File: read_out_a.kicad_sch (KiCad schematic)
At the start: 26 parts, among them J1 Bus_PCI_Express_x16, U10 74LS541, U11 74LS541, U12 74LS541, U13 74LS541, U14 74LS541, U15 74LS541, U16 74LS541, U17 74LS30, U18 74LS04, U9 74LS541

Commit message: Current progress.  Working on laying out the latched bus.
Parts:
- C12: renamed from C9; footprint (none) -> Capacitor_SMD:C_0805_2012Metric_Pad1.18x1.45mm_HandSolder
- C13: renamed from C10; footprint (none) -> Capacitor_SMD:C_0805_2012Metric_Pad1.18x1.45mm_HandSolder
- C14: renamed from C11; footprint (none) -> Capacitor_SMD:C_0805_2012Metric_Pad1.18x1.45mm_HandSolder
- C15: renamed from C12; footprint (none) -> Capacitor_SMD:C_0805_2012Metric_Pad1.18x1.45mm_HandSolder
- C16: renamed from C13; footprint (none) -> Capacitor_SMD:C_0805_2012Metric_Pad1.18x1.45mm_HandSolder
- C17: renamed from C14; footprint (none) -> Capacitor_SMD:C_0805_2012Metric_Pad1.18x1.45mm_HandSolder
- C18: renamed from C15; footprint (none) -> Capacitor_SMD:C_0805_2012Metric_Pad1.18x1.45mm_HandSolder
- C19: renamed from C16; footprint (none) -> Capacitor_SMD:C_0805_2012Metric_Pad1.18x1.45mm_HandSolder
- C20: renamed from C17; footprint (none) -> Capacitor_SMD:C_0805_2012Metric_Pad1.18x1.45mm_HandSolder
- C21: renamed from C18; footprint (none) -> Capacitor_SMD:C_0805_2012Metric_Pad1.18x1.45mm_HandSolder
- JP10: renamed from JP5; footprint (none) -> Jumper:SolderJumper-3_P1.3mm_Open_RoundedPad1.0x1.5mm
- JP6: renamed from JP1; footprint (none) -> Jumper:SolderJumper-3_P1.3mm_Open_RoundedPad1.0x1.5mm
- JP7: renamed from JP2; footprint (none) -> Jumper:SolderJumper-3_P1.3mm_Open_RoundedPad1.0x1.5mm
- JP8: renamed from JP3; footprint (none) -> Jumper:SolderJumper-3_P1.3mm_Open_RoundedPad1.0x1.5mm
- JP9: renamed from JP4; footprint (none) -> Jumper:SolderJumper-3_P1.3mm_Open_RoundedPad1.0x1.5mm
- U12: renamed from U9; footprint (none) -> Package_SO:SOIC-20W_7.5x12.8mm_P1.27mm
- U13: renamed from U10; footprint (none) -> Package_SO:SOIC-20W_7.5x12.8mm_P1.27mm
- U14: renamed from U11; footprint (none) -> Package_SO:SOIC-20W_7.5x12.8mm_P1.27mm
- U15: renamed from U12; footprint (none) -> Package_SO:SOIC-20W_7.5x12.8mm_P1.27mm
- U16: renamed from U13; footprint (none) -> Package_SO:SOIC-20W_7.5x12.8mm_P1.27mm
- U17: renamed from U14; footprint (none) -> Package_SO:SOIC-20W_7.5x12.8mm_P1.27mm
- U18: renamed from U15; footprint (none) -> Package_SO:SOIC-20W_7.5x12.8mm_P1.27mm
- U19: renamed from U16; footprint (none) -> Package_SO:SOIC-20W_7.5x12.8mm_P1.27mm
- U20: renamed from U18; footprint (none) -> Package_SO:SOIC-14_3.9x8.7mm_P1.27mm
- U21: renamed from U17; footprint (none) -> Package_SO:SOIC-14_3.9x8.7mm_P1.27mm
- renumbered J1 to J2
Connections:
- net CLK_PH0: no longer names the net of J2.A13 (REFCLK+)
- net CLK_PH1: no longer names the net of J2.A14 (REFCLK-)
- net latched00 renamed latched0
- net latched01 renamed latched1
- net latched02 renamed latched2
- net latched03 renamed latched3
- net latched04 renamed latched4
- net latched05 renamed latched5
- net latched06 renamed latched6
- net latched07 renamed latched7
- net latched08 renamed latched8
- net latched09 renamed latched9
- net read_a00 renamed read_a0
- net read_a01 renamed read_a1
- net read_a02 renamed read_a2
- net read_a03 renamed read_a3
- net read_a04 renamed read_a4
- net read_a05 renamed read_a5
- net read_a06 renamed read_a6
- net read_a07 renamed read_a7
- net read_a08 renamed read_a8
- net read_a09 renamed read_a9
- net ~{RST}: no longer names the net of J2.A11 (~{PERST})
- no-connect marks 17 -> 20

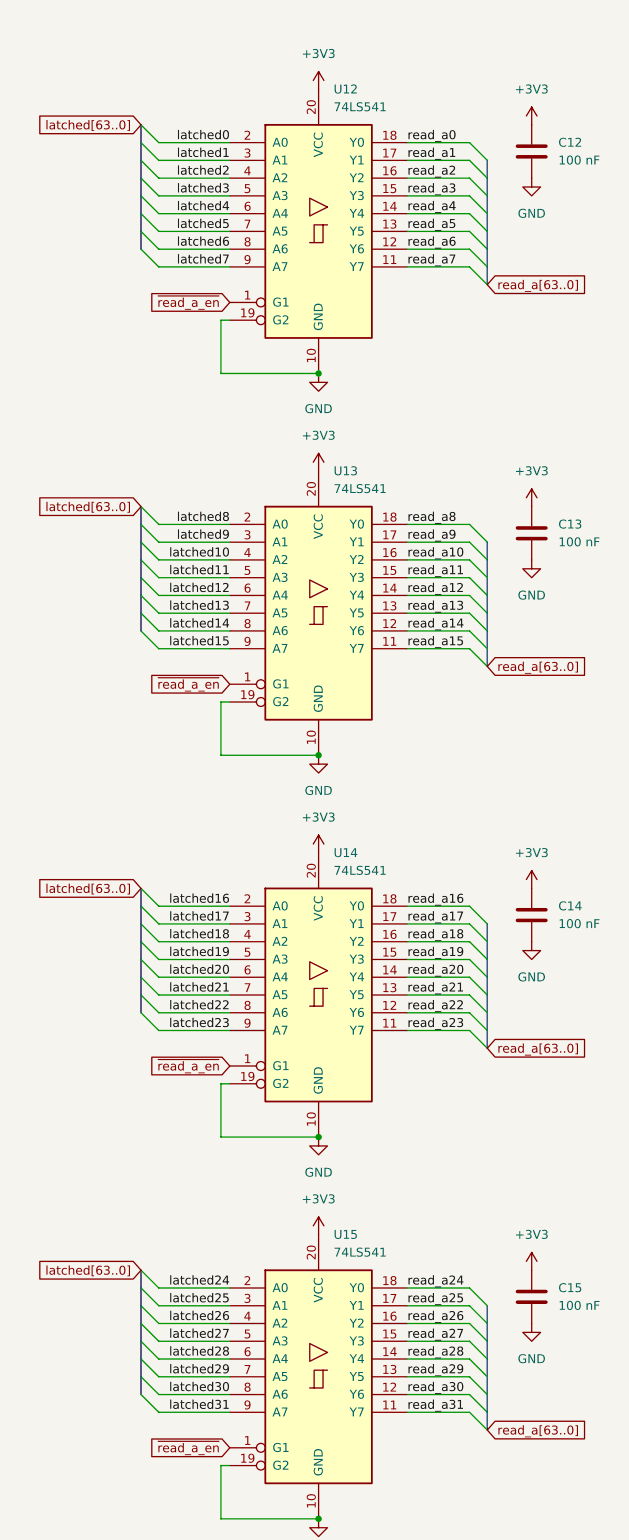
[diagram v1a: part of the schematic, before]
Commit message: Read A Port mostly routed.
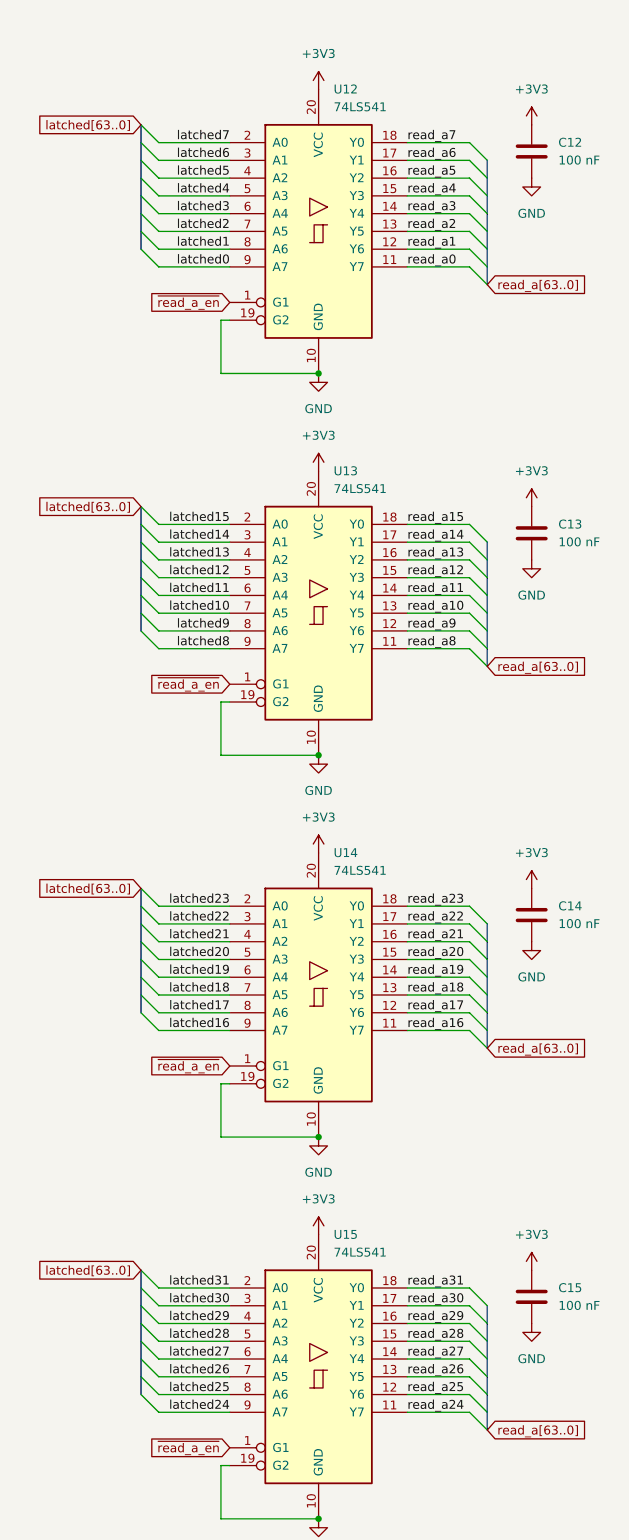
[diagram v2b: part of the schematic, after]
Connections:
- net latched0: now also U12.9 (A7); no longer U12.2 (A0)
- net latched1: now also U12.8 (A6); no longer U12.3 (A1)
- net latched10: now also U13.7 (A5); no longer U13.4 (A2)
- net latched11: now also U13.6 (A4); no longer U13.5 (A3)
- net latched12: now also U13.5 (A3); no longer U13.6 (A4)
- net latched13: now also U13.4 (A2); no longer U13.7 (A5)
- net latched14: now also U13.3 (A1); no longer U13.8 (A6)
- net latched15: now also U13.2 (A0); no longer U13.9 (A7)
- net latched16: now also U14.9 (A7); no longer U14.2 (A0)
- net latched17: now also U14.8 (A6); no longer U14.3 (A1)
- net latched18: now also U14.7 (A5); no longer U14.4 (A2)
- net latched19: now also U14.6 (A4); no longer U14.5 (A3)
- net latched2: now also U12.7 (A5); no longer U12.4 (A2)
- net latched20: now also U14.5 (A3); no longer U14.6 (A4)
- net latched21: now also U14.4 (A2); no longer U14.7 (A5)
- net latched22: now also U14.3 (A1); no longer U14.8 (A6)
- net latched23: now also U14.2 (A0); no longer U14.9 (A7)
- net latched24: now also U15.9 (A7); no longer U15.2 (A0)
- net latched25: now also U15.8 (A6); no longer U15.3 (A1)
- net latched26: now also U15.7 (A5); no longer U15.4 (A2)
- net latched27: now also U15.6 (A4); no longer U15.5 (A3)
- net latched28: now also U15.5 (A3); no longer U15.6 (A4)
- net latched29: now also U15.4 (A2); no longer U15.7 (A5)
- net latched3: now also U12.6 (A4); no longer U12.5 (A3)
- net latched30: now also U15.3 (A1); no longer U15.8 (A6)
- net latched31: now also U15.2 (A0); no longer U15.9 (A7)
- net latched4: now also U12.5 (A3); no longer U12.6 (A4)
- net latched5: now also U12.4 (A2); no longer U12.7 (A5)
- net latched6: now also U12.3 (A1); no longer U12.8 (A6)
- net latched7: now also U12.2 (A0); no longer U12.9 (A7)
- net latched8: now also U13.9 (A7); no longer U13.2 (A0)
- net latched9: now also U13.8 (A6); no longer U13.3 (A1)
- net read_a0: now also U12.11 (Y7); no longer U12.18 (Y0)
- net read_a1: now also U12.12 (Y6); no longer U12.17 (Y1)
- net read_a10: now also U13.13 (Y5); no longer U13.16 (Y2)
- net read_a11: now also U13.14 (Y4); no longer U13.15 (Y3)
- net read_a12: now also U13.15 (Y3); no longer U13.14 (Y4)
- net read_a13: now also U13.16 (Y2); no longer U13.13 (Y5)
- net read_a14: now also U13.17 (Y1); no longer U13.12 (Y6)
- net read_a15: now also U13.18 (Y0); no longer U13.11 (Y7)
- net read_a16: now also U14.11 (Y7); no longer U14.18 (Y0)
- net read_a17: now also U14.12 (Y6); no longer U14.17 (Y1)
- net read_a18: now also U14.13 (Y5); no longer U14.16 (Y2)
- net read_a19: now also U14.14 (Y4); no longer U14.15 (Y3)
- net read_a2: now also U12.13 (Y5); no longer U12.16 (Y2)
- net read_a20: now also U14.15 (Y3); no longer U14.14 (Y4)
- net read_a21: now also U14.16 (Y2); no longer U14.13 (Y5)
- net read_a22: now also U14.17 (Y1); no longer U14.12 (Y6)
- net read_a23: now also U14.18 (Y0); no longer U14.11 (Y7)
- net read_a24: now also U15.11 (Y7); no longer U15.18 (Y0)
- net read_a25: now also U15.12 (Y6); no longer U15.17 (Y1)
- net read_a26: now also U15.13 (Y5); no longer U15.16 (Y2)
- net read_a27: now also U15.14 (Y4); no longer U15.15 (Y3)
- net read_a28: now also U15.15 (Y3); no longer U15.14 (Y4)
- net read_a29: now also U15.16 (Y2); no longer U15.13 (Y5)
- net read_a3: now also U12.14 (Y4); no longer U12.15 (Y3)
- net read_a30: now also U15.17 (Y1); no longer U15.12 (Y6)
- net read_a31: now also U15.18 (Y0); no longer U15.11 (Y7)
- net read_a4: now also U12.15 (Y3); no longer U12.14 (Y4)
- net read_a5: now also U12.16 (Y2); no longer U12.13 (Y5)
- net read_a6: now also U12.17 (Y1); no longer U12.12 (Y6)
- net read_a7: now also U12.18 (Y0); no longer U12.11 (Y7)
- net read_a8: now also U13.11 (Y7); no longer U13.18 (Y0)
- net read_a9: now also U13.12 (Y6); no longer U13.17 (Y1)
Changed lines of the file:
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@@
 	)
 	(label "latched6"
-		(at 73.66 53.34 180)
+		(at 73.66 40.64 180)
 		(effects
 			(font
@@
 	)
 	(label "latched29"
-		(at 73.66 214.63 180)
+		(at 73.66 207.01 180)
 		(effects
 			(font
@@
 	)
 	(label "latched18"
-		(at 73.66 152.4 180)
+		(at 73.66 160.02 180)
 		(effects
 			(font
@@
 	)
 	(label "read_a6"
-		(at 99.06 53.34 0)
+		(at 99.06 40.64 0)
 		(effects
 			(font
@@
 	)
 	(label "read_a0"
-		(at 99.06 38.1 0)
+		(at 99.06 55.88 0)
 		(effects
 			(font
@@
 	)
 	(label "latched12"
-		(at 73.66 102.87 180)
+		(at 73.66 100.33 180)
 		(effects
 			(font
@@
 	)
 	(label "read_a5"
-		(at 99.06 50.8 0)
+		(at 99.06 43.18 0)
 		(effects
 			(font
@@
 	)
 	(label "latched14"
-		(at 73.66 107.95 180)
+		(at 73.66 95.25 180)
 		(effects
 			(font
@@
 	)
 	(label "read_a9"
-		(at 99.06 95.25 0)
+		(at 99.06 107.95 0)
 		(effects
 			(font
@@
 	)
 	(label "read_a15"
-		(at 99.06 110.49 0)
+		(at 99.06 92.71 0)
 		(effects
 			(font
@@
 	)
 	(label "latched15"
-		(at 73.66 110.49 180)
+		(at 73.66 92.71 180)
 		(effects
 			(font
@@
 	)
 	(label "latched17"
-		(at 73.66 149.86 180)
+		(at 73.66 162.56 180)
 		(effects
 			(font
@@
 	)
 	(label "latched27"
-		(at 73.66 209.55 180)
+		(at 73.66 212.09 180)
 		(effects
 			(font
@@
 	)
 	(label "latched13"
-		(at 73.66 105.41 180)
+		(at 73.66 97.79 180)
 		(effects
 			(font
@@
 	)
 	(label "latched19"
-		(at 73.66 154.94 180)
+		(at 73.66 157.48 180)
 		(effects
 			(font
@@
 	)
 	(label "latched9"
-		(at 73.66 95.25 180)
+		(at 73.66 107.95 180)
 		(effects
 			(font
@@
 	)
 	(label "read_a12"
-		(at 99.06 102.87 0)
+		(at 99.06 100.33 0)
 		(effects
 			(font
@@
 	)
 	(label "latched7"
-		(at 73.66 55.88 180)
+		(at 73.66 38.1 180)
 		(effects
 			(font
@@
 	)
 	(label "latched28"
-		(at 73.66 212.09 180)
+		(at 73.66 209.55 180)
 		(effects
 			(font
@@
 	)
 	(label "latched24"
-		(at 73.66 201.93 180)
+		(at 73.66 219.71 180)
 		(effects
 			(font
@@
 	)
 	(label "read_a7"
-		(at 99.06 55.88 0)
+		(at 99.06 38.1 0)
 		(effects
 			(font
@@
 	)
 	(label "latched11"
-		(at 73.66 100.33 180)
+		(at 73.66 102.87 180)
 		(effects
 			(font
@@
 	)
 	(label "read_a13"
-		(at 99.06 105.41 0)
+		(at 99.06 97.79 0)
 		(effects
 			(font
@@
 	)
 	(label "read_a28"
-		(at 99.06 212.09 0)
+		(at 99.06 209.55 0)
 		(effects
 			(font
@@
 	)
 	(label "latched20"
-		(at 73.66 157.48 180)
+		(at 73.66 154.94 180)
 		(effects
 			(font
@@
 	)
 	(label "read_a10"
-		(at 99.06 97.79 0)
+		(at 99.06 105.41 0)
 		(effects
 			(font
@@
 	)
 	(label "latched22"
-		(at 73.66 162.56 180)
+		(at 73.66 149.86 180)
 		(effects
 			(font
@@
 	)
 	(label "latched21"
-		(at 73.66 160.02 180)
+		(at 73.66 152.4 180)
 		(effects
 			(font
@@
 	)
 	(label "latched5"
-		(at 73.66 50.8 180)
+		(at 73.66 43.18 180)
 		(effects
 			(font
@@
 	)
 	(label "read_a11"
-		(at 99.06 100.33 0)
+		(at 99.06 102.87 0)
 		(effects
 			(font
@@
 	)
 	(label "latched8"
-		(at 73.66 92.71 180)
+		(at 73.66 110.49 180)
 		(effects
 			(font
@@
 	)
 	(label "latched16"
-		(at 73.66 147.32 180)
+		(at 73.66 165.1 180)
 		(effects
 			(font
@@
 	)
 	(label "read_a29"
-		(at 99.06 214.63 0)
+		(at 99.06 207.01 0)
 		(effects
 			(font
@@
 	)
 	(label "read_a2"
-		(at 99.06 43.18 0)
+		(at 99.06 50.8 0)
 		(effects
 			(font
@@
 	)
 	(label "read_a17"
-		(at 99.06 149.86 0)
+		(at 99.06 162.56 0)
 		(effects
 			(font
@@
 	)
 	(label "latched3"
-		(at 73.66 45.72 180)
+		(at 73.66 48.26 180)
 		(effects
 			(font
@@
 	)
 	(label "latched10"
-		(at 73.66 97.79 180)
+		(at 73.66 105.41 180)
 		(effects
 			(font
@@
 	)
 	(label "latched0"
-		(at 73.66 38.1 180)
+		(at 73.66 55.88 180)
 		(effects
 			(font
@@
 	)
 	(label "latched25"
-		(at 73.66 204.47 180)
+		(at 73.66 217.17 180)
 		(effects
 			(font
@@
 	)
 	(label "latched26"
-		(at 73.66 207.01 180)
+		(at 73.66 214.63 180)
 		(effects
 			(font
@@
 	)
 	(label "read_a31"
-		(at 99.06 219.71 0)
+		(at 99.06 201.93 0)
 		(effects
 			(font
@@
 	)
 	(label "read_a8"
-		(at 99.06 92.71 0)
+		(at 99.06 110.49 0)
 		(effects
 			(font
@@
 	)
 	(label "read_a16"
-		(at 99.06 147.32 0)
+		(at 99.06 165.1 0)
 		(effects
 			(font
@@
 	)
 	(label "read_a1"
-		(at 99.06 40.64 0)
+		(at 99.06 53.34 0)
 		(effects
 			(font
@@
 	)
 	(label "read_a23"
-		(at 99.06 165.1 0)
+		(at 99.06 147.32 0)
 		(effects
 			(font
@@
 	)
 	(label "read_a30"
-		(at 99.06 217.17 0)
+		(at 99.06 204.47 0)
 		(effects
 			(font
@@
 	)
 	(label "read_a24"
-		(at 99.06 201.93 0)
+		(at 99.06 219.71 0)
 		(effects
 			(font
@@
 	)
 	(label "latched4"
-		(at 73.66 48.26 180)
+		(at 73.66 45.72 180)
 		(effects
 			(font
@@
 	)
 	(label "read_a19"
-		(at 99.06 154.94 0)
+		(at 99.06 157.48 0)
 		(effects
 			(font
@@
 	)
 	(label "latched23"
-		(at 73.66 165.1 180)
+		(at 73.66 147.32 180)
 		(effects
 			(font
@@
 	)
 	(label "read_a27"
-		(at 99.06 209.55 0)
+		(at 99.06 212.09 0)
 		(effects
 			(font
@@
 	)
 	(label "read_a20"
-		(at 99.06 157.48 0)
+		(at 99.06 154.94 0)
 		(effects
 			(font
@@
 	)
 	(label "latched1"
-		(at 73.66 40.64 180)
+		(at 73.66 53.34 180)
 		(effects
 			(font
@@
 	)
 	(label "read_a25"
-		(at 99.06 204.47 0)
+		(at 99.06 217.17 0)
 		(effects
 			(font
@@
 	)
 	(label "latched30"
-		(at 73.66 217.17 180)
+		(at 73.66 204.47 180)
 		(effects
 			(font
@@
 	)
 	(label "latched2"
-		(at 73.66 43.18 180)
+		(at 73.66 50.8 180)
 		(effects
 			(font
@@
 	)
 	(label "read_a14"
-		(at 99.06 107.95 0)
+		(at 99.06 95.25 0)
 		(effects
 			(font
@@
 	)
 	(label "read_a18"
-		(at 99.06 152.4 0)
+		(at 99.06 160.02 0)
 		(effects
 			(font
@@
 	)
 	(label "read_a4"
-		(at 99.06 48.26 0)
+		(at 99.06 45.72 0)
 		(effects
 			(font
@@
 	)
 	(label "read_a21"
-		(at 99.06 160.02 0)
+		(at 99.06 152.4 0)
 		(effects
 			(font
@@
 	)
 	(label "read_a26"
-		(at 99.06 207.01 0)
+		(at 99.06 214.63 0)
 		(effects
 			(font
@@
 	)
 	(label "read_a3"
-		(at 99.06 45.72 0)
+		(at 99.06 48.26 0)
 		(effects
 			(font
@@
 	)
 	(label "read_a22"
-		(at 99.06 162.56 0)
+		(at 99.06 149.86 0)
 		(effects
 			(font
@@
 	)
 	(label "latched31"
-		(at 73.66 219.71 180)
-		(effects
-			(font
+		(at 73.66 201.93 180)
+		(effects
+			(font

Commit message: Getting close to done with Read A Port.
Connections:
- net read_a_en: now also U20.6; no longer U20.12
- net read_a_sel2: now also U20.13; no longer U20.5
- net read_a_sel3: now also U20.11; no longer U20.9
- net read_a_sel4: now also U20.9; no longer U20.11
- net ~{read_a_en}: now also U20.5; no longer U20.13
- net at U20.8: now also JP10.3 (B); no longer JP9.3 (B)
- net at JP8.3 (B): now also U20.12; no longer U20.6
- net at U20.10: now also JP9.3 (B); no longer JP10.3 (B)
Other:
- moved on the sheet: U20C, U20D, U20E, U20F
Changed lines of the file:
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@@
 	(symbol
 		(lib_id "74xx:74LS04")
-		(at 265.43 129.54 0)
+		(at 265.43 158.75 0)
 		(unit 4)
 		(exclude_from_sim no)
@@
 		(fields_autoplaced yes)
 		(property "Reference" "U20"
-			(at 265.43 120.65 0)
+			(at 265.43 149.86 0)
 			(effects
 				(font
@@
 		)
 		(property "Value" "74LS04"
-			(at 265.43 123.19 0)
+			(at 265.43 152.4 0)
 			(effects
 				(font
@@
 		)
 		(property "Footprint" "Package_SO:SOIC-14_3.9x8.7mm_P1.27mm"
-			(at 265.43 129.54 0)
+			(at 265.43 158.75 0)
 			(effects
 				(font
@@
 		)
 		(property "Datasheet" "http://www.ti.com/lit/gpn/sn74LS04"
-			(at 265.43 129.54 0)
+			(at 265.43 158.75 0)
 			(effects
 				(font
@@
 		)
 		(property "Description" "Hex Inverter"
-			(at 265.43 129.54 0)
+			(at 265.43 158.75 0)
 			(effects
 				(font
@@
 	(symbol
 		(lib_id "74xx:74LS04")
-		(at 265.43 100.33 0)
+		(at 321.31 38.1 0)
 		(unit 3)
 		(exclude_from_sim no)
@@
 		(fields_autoplaced yes)
 		(property "Reference" "U20"
-			(at 265.43 91.44 0)
+			(at 321.31 29.21 0)
 			(effects
 				(font
@@
 		)
 		(property "Value" "74LS04"
-			(at 265.43 93.98 0)
+			(at 321.31 31.75 0)
 			(effects
 				(font
@@
 		)
 		(property "Footprint" "Package_SO:SOIC-14_3.9x8.7mm_P1.27mm"
-			(at 265.43 100.33 0)
+			(at 321.31 38.1 0)
 			(effects
 				(font
@@
 		)
 		(property "Datasheet" "http://www.ti.com/lit/gpn/sn74LS04"
-			(at 265.43 100.33 0)
+			(at 321.31 38.1 0)
 			(effects
 				(font
@@
 		)
 		(property "Description" "Hex Inverter"
-			(at 265.43 100.33 0)
+			(at 321.31 38.1 0)
 			(effects
 				(font
@@
 	(symbol
 		(lib_id "74xx:74LS04")
-		(at 265.43 158.75 0)
+		(at 265.43 129.54 0)
 		(unit 5)
 		(exclude_from_sim no)
@@
 		(fields_autoplaced yes)
 		(property "Reference" "U20"
-			(at 265.43 149.86 0)
+			(at 265.43 120.65 0)
 			(effects
 				(font
@@
 		)
 		(property "Value" "74LS04"
-			(at 265.43 152.4 0)
+			(at 265.43 123.19 0)
 			(effects
 				(font
@@
 		)
 		(property "Footprint" "Package_SO:SOIC-14_3.9x8.7mm_P1.27mm"
-			(at 265.43 158.75 0)
+			(at 265.43 129.54 0)
 			(effects
 				(font
@@
 		)
 		(property "Datasheet" "http://www.ti.com/lit/gpn/sn74LS04"
-			(at 265.43 158.75 0)
+			(at 265.43 129.54 0)
 			(effects
 				(font
@@
 		)
 		(property "Description" "Hex Inverter"
-			(at 265.43 158.75 0)
+			(at 265.43 129.54 0)
 			(effects
 				(font
@@
 	(symbol
 		(lib_id "74xx:74LS04")
-		(at 321.31 38.1 0)
+		(at 265.43 100.33 0)
 		(unit 6)
 		(exclude_from_sim no)
@@
 		(fields_autoplaced yes)
 		(property "Reference" "U20"
-			(at 321.31 29.21 0)
+			(at 265.43 91.44 0)
 			(effects
 				(font
@@
 		)
 		(property "Value" "74LS04"
-			(at 321.31 31.75 0)
+			(at 265.43 93.98 0)
 			(effects
 				(font
@@
 		)
 		(property "Footprint" "Package_SO:SOIC-14_3.9x8.7mm_P1.27mm"
-			(at 321.31 38.1 0)
+			(at 265.43 100.33 0)
 			(effects
 				(font
@@
 		)
 		(property "Datasheet" "http://www.ti.com/lit/gpn/sn74LS04"
-			(at 321.31 38.1 0)
+			(at 265.43 100.33 0)
 			(effects
 				(font
@@
 		)
 		(property "Description" "Hex Inverter"
-			(at 321.31 38.1 0)
+			(at 265.43 100.33 0)
 			(effects
 				(font
